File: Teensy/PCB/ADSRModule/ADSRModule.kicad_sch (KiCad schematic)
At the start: 14 parts, among them J1 Conn_02x03_Odd_Even, SW1 SW_SPDT_MSM, U1 Teensy4.0

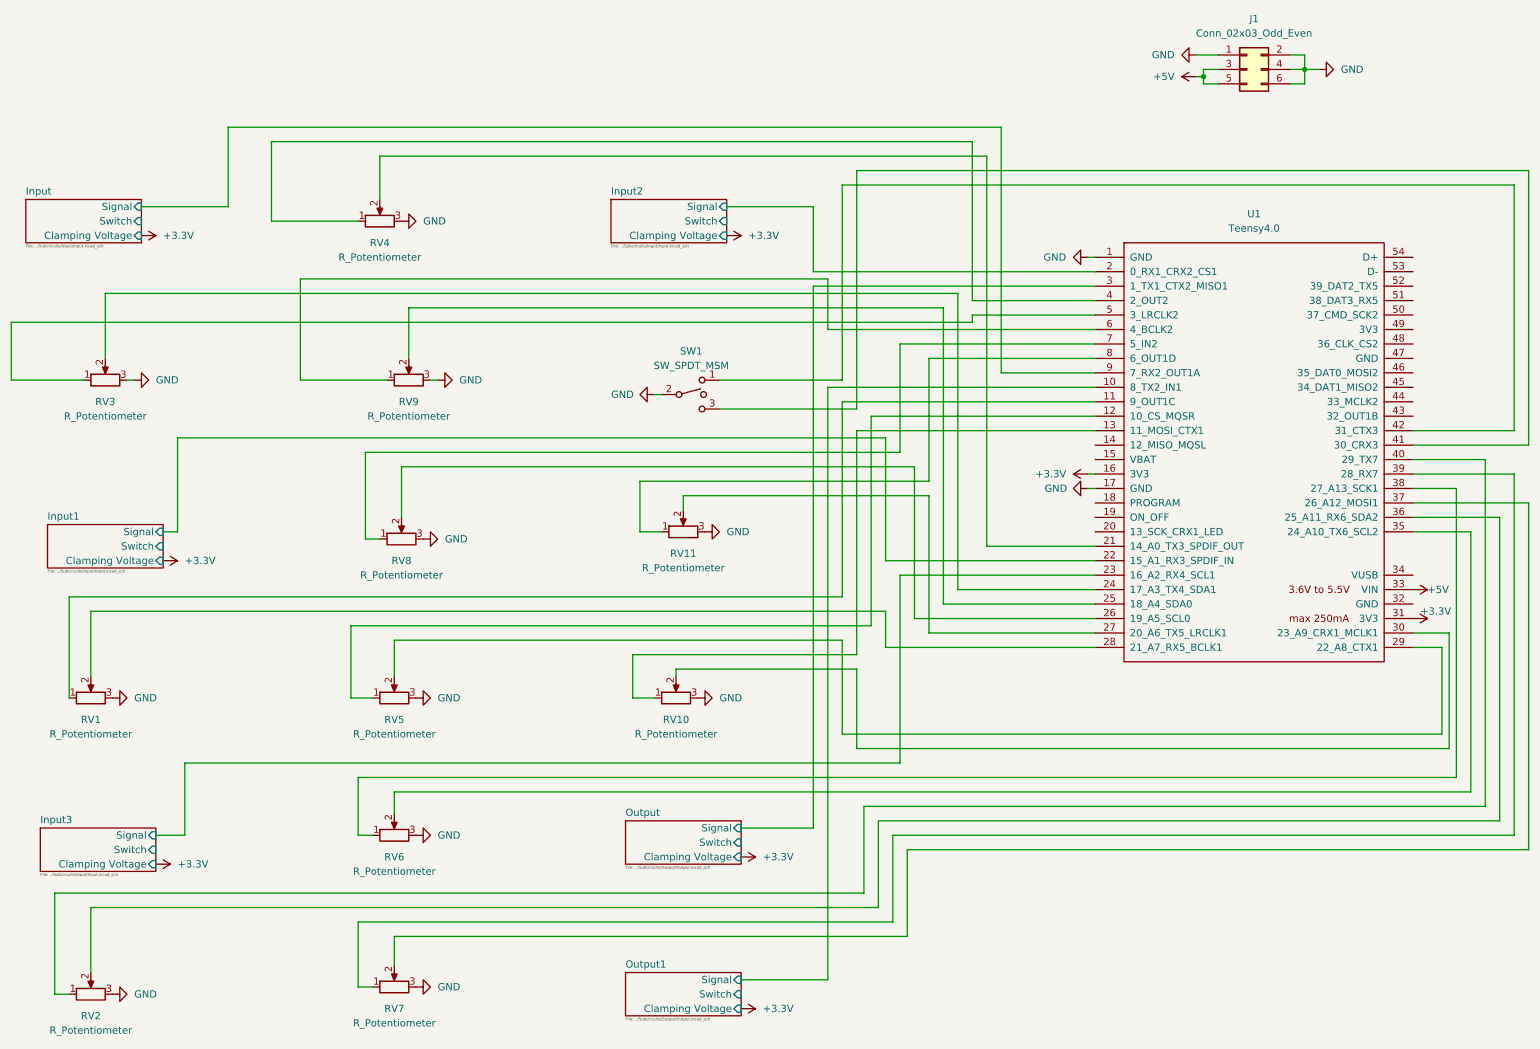
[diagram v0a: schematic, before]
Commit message: Fixed component names on schematic
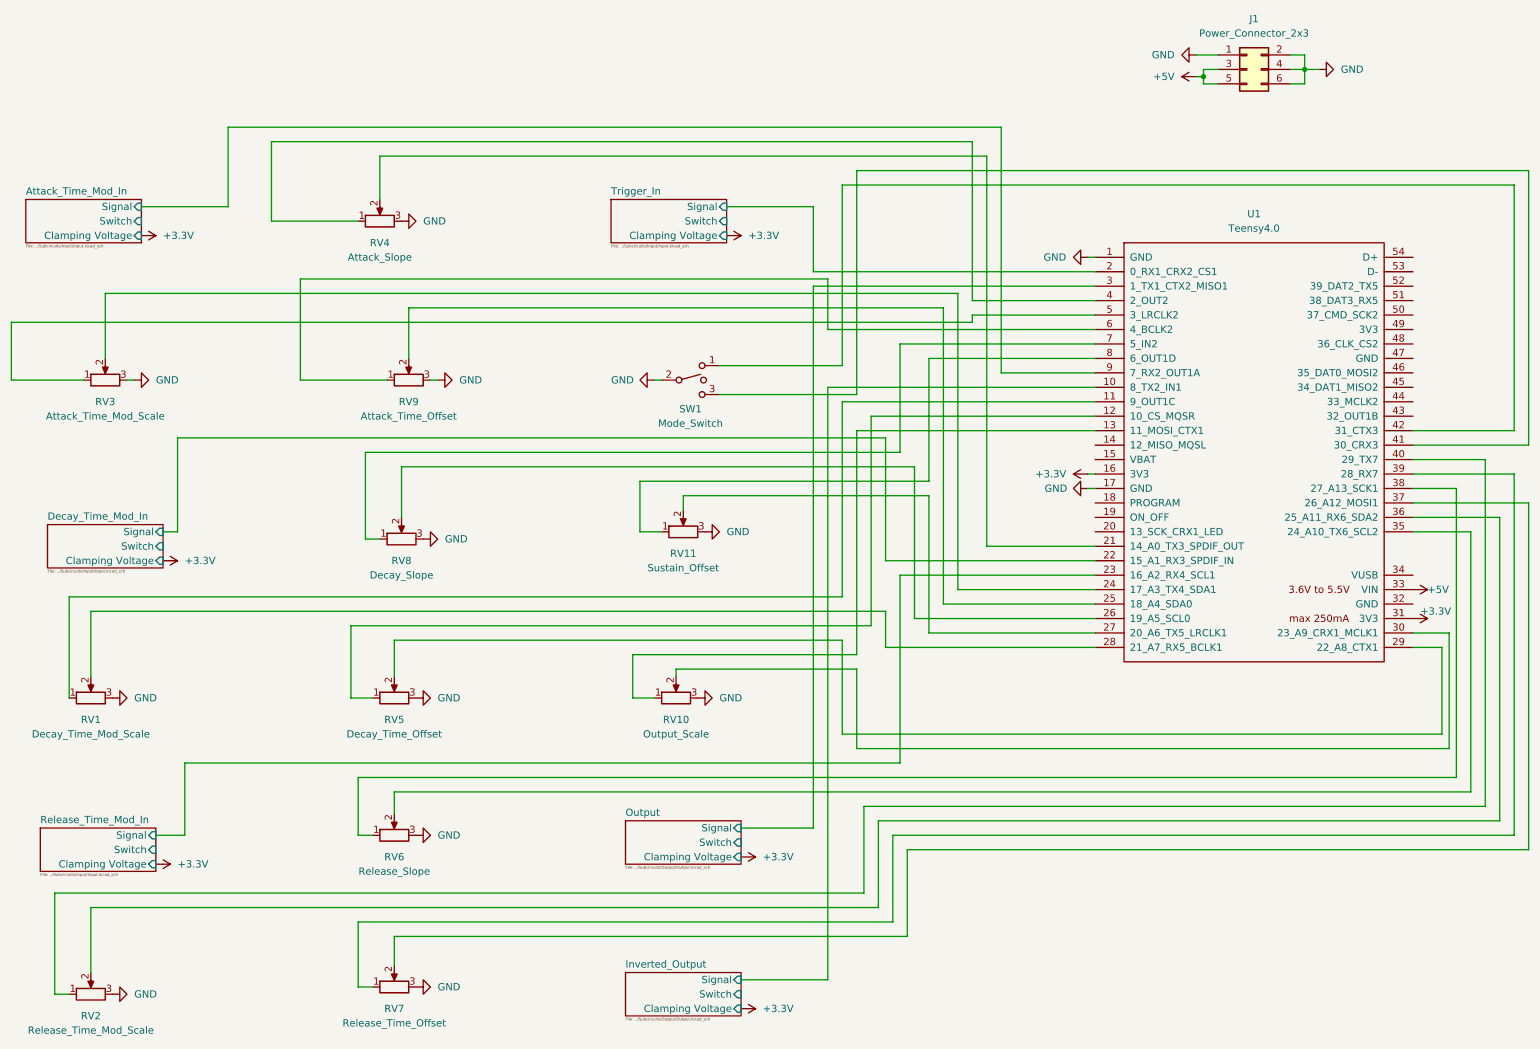
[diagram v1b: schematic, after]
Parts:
- J1: value Conn_02x03_Odd_Even -> Power_Connector_2x3
- RV1: value R_Potentiometer -> Decay_Time_Mod_Scale
- RV10: value R_Potentiometer -> Output_Scale
- RV11: value R_Potentiometer -> Sustain_Offset
- RV2: value R_Potentiometer -> Release_Time_Mod_Scale
- RV3: value R_Potentiometer -> Attack_Time_Mod_Scale
- RV4: value R_Potentiometer -> Attack_Slope
- RV5: value R_Potentiometer -> Decay_Time_Offset
- RV6: value R_Potentiometer -> Release_Slope
- RV7: value R_Potentiometer -> Release_Time_Offset
- RV8: value R_Potentiometer -> Decay_Slope
- RV9: value R_Potentiometer -> Attack_Time_Offset
- SW1: value SW_SPDT_MSM -> Mode_Switch
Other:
- sheet Input renamed Attack_Time_Mod_In
- sheet Input1 renamed Decay_Time_Mod_In
- sheet Input2 renamed Trigger_In
- sheet Input3 renamed Release_Time_Mod_In
- sheet Output1 renamed Inverted_Output
- moved on the sheet: SW1

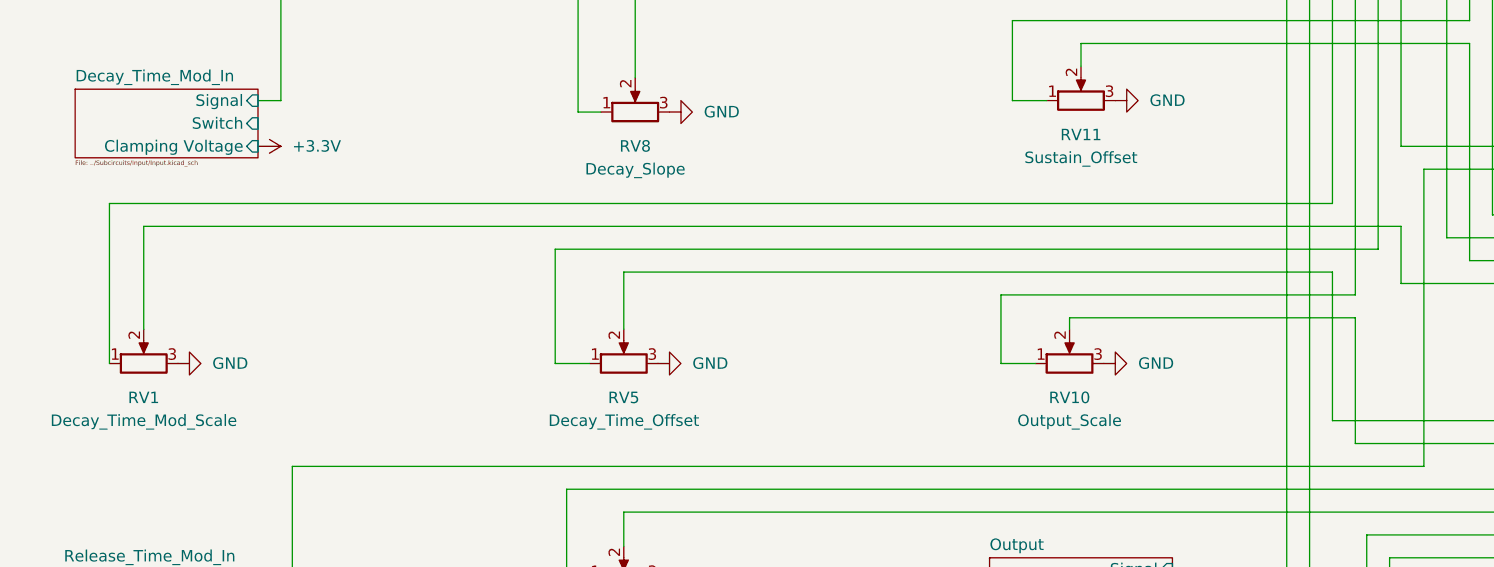
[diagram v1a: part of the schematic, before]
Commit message: Added USB_IO module PCB
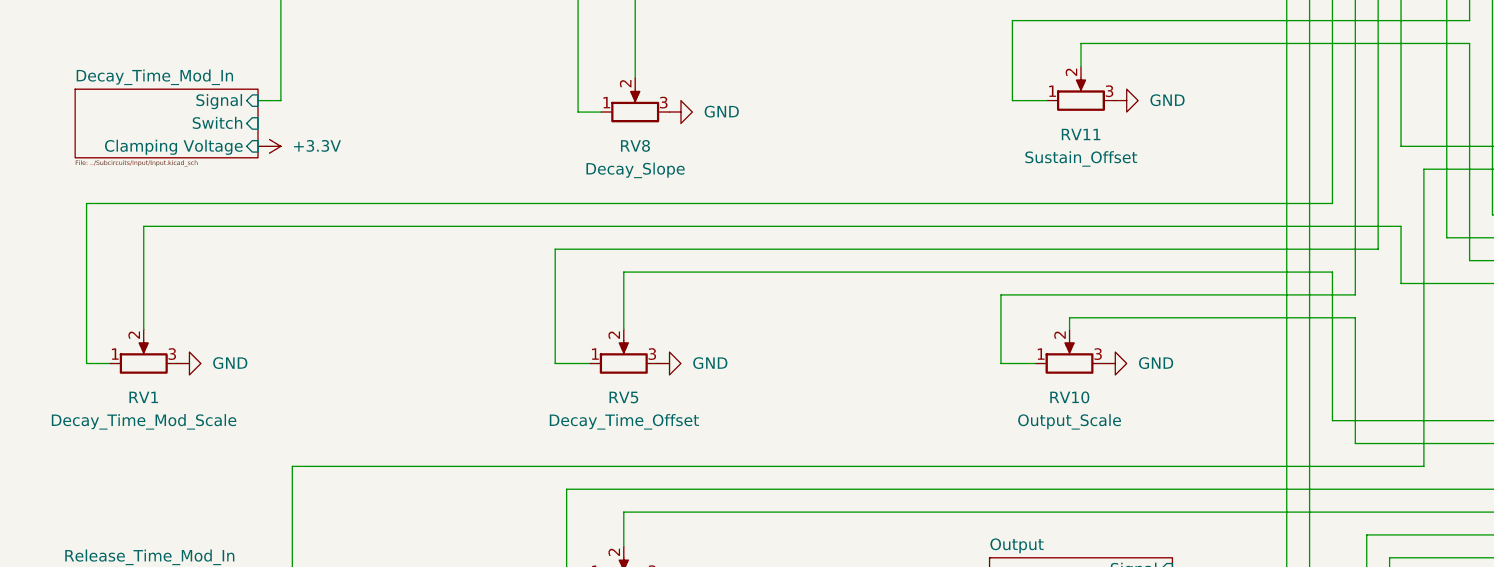
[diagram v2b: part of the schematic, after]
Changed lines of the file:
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@@
     (stroke (width 0) (type default) (color 0 0 0 0))
   )
-  (wire (pts (xy 25.4 137.16) (xy 25.4 119.38))
+  (wire (pts (xy 22.86 137.16) (xy 22.86 119.38))
     (stroke (width 0) (type default) (color 0 0 0 0))
   )
@@
     (stroke (width 0) (type default) (color 0 0 0 0))
   )
+  (wire (pts (xy 22.86 137.16) (xy 25.4 137.16))
+    (stroke (width 0) (type default) (color 0 0 0 0))
+  )
   (wire (pts (xy 35.56 81.28) (xy 36.83 81.28))
     (stroke (width 0) (type default) (color 0 0 0 0))
@@
     (stroke (width 0) (type default) (color 0 0 0 0))
   )
-  (wire (pts (xy 25.4 119.38) (xy 161.29 119.38))
-    (stroke (width 0) (type default) (color 0 0 0 0))
-  )
+  (wire (pts (xy 22.86 119.38) (xy 161.29 119.38))
+    (stroke (width 0) (type default) (color 0 0 0 0))
+  )

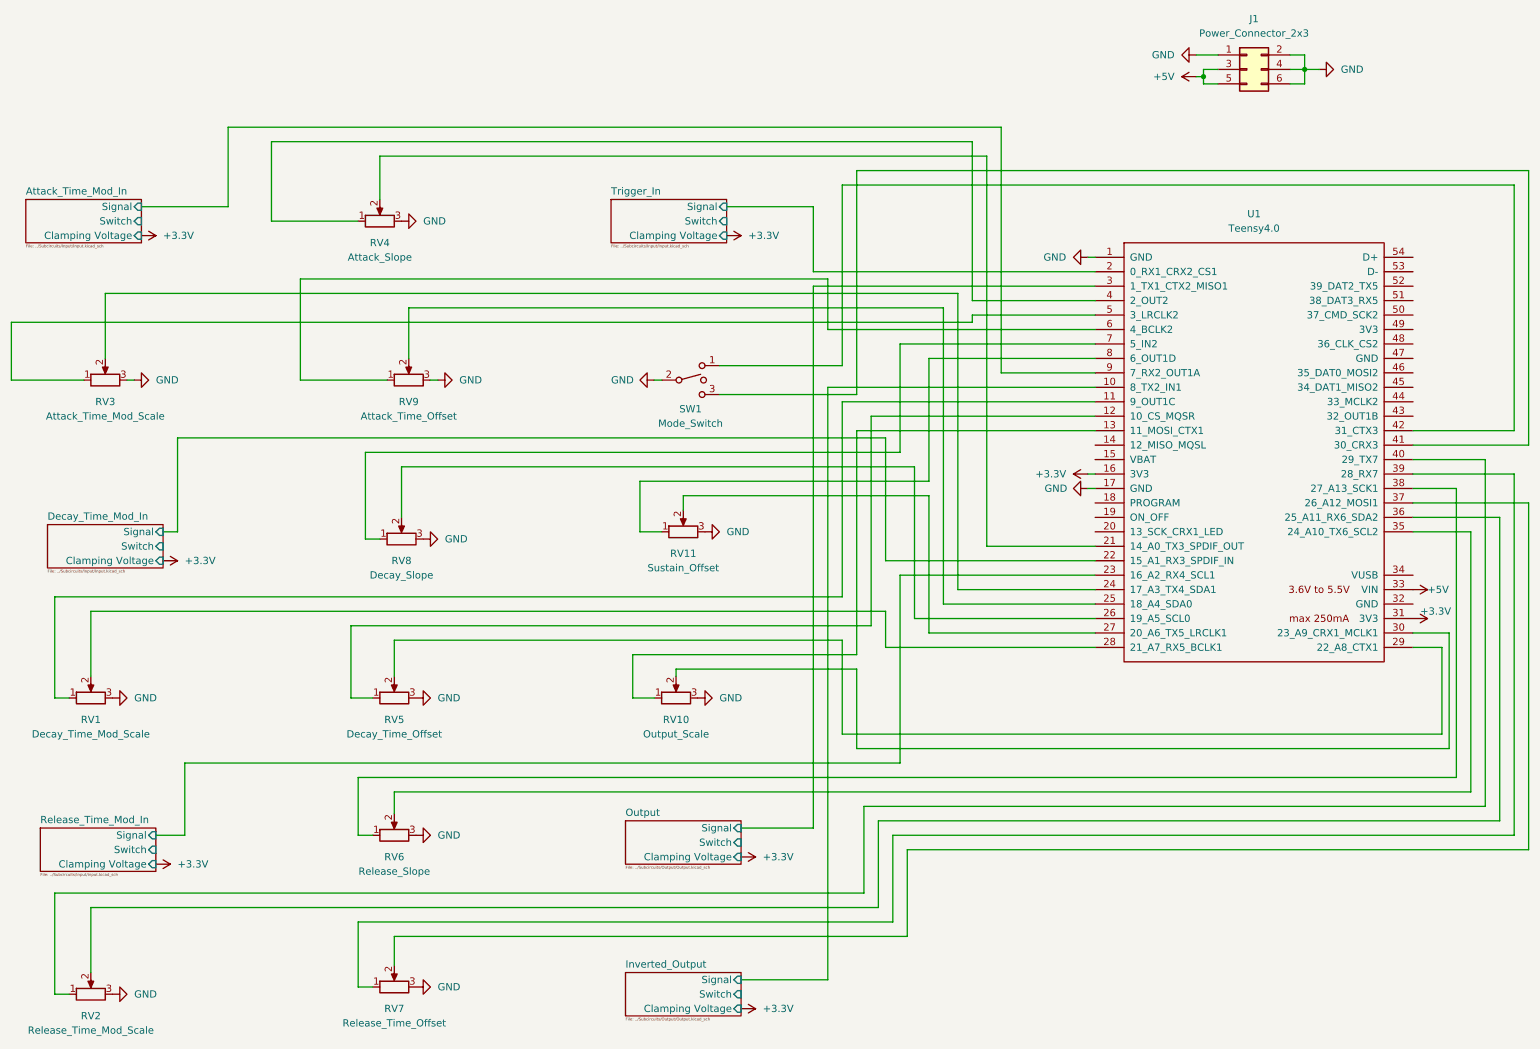
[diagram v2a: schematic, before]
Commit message: Replaced Schematic Lines with references
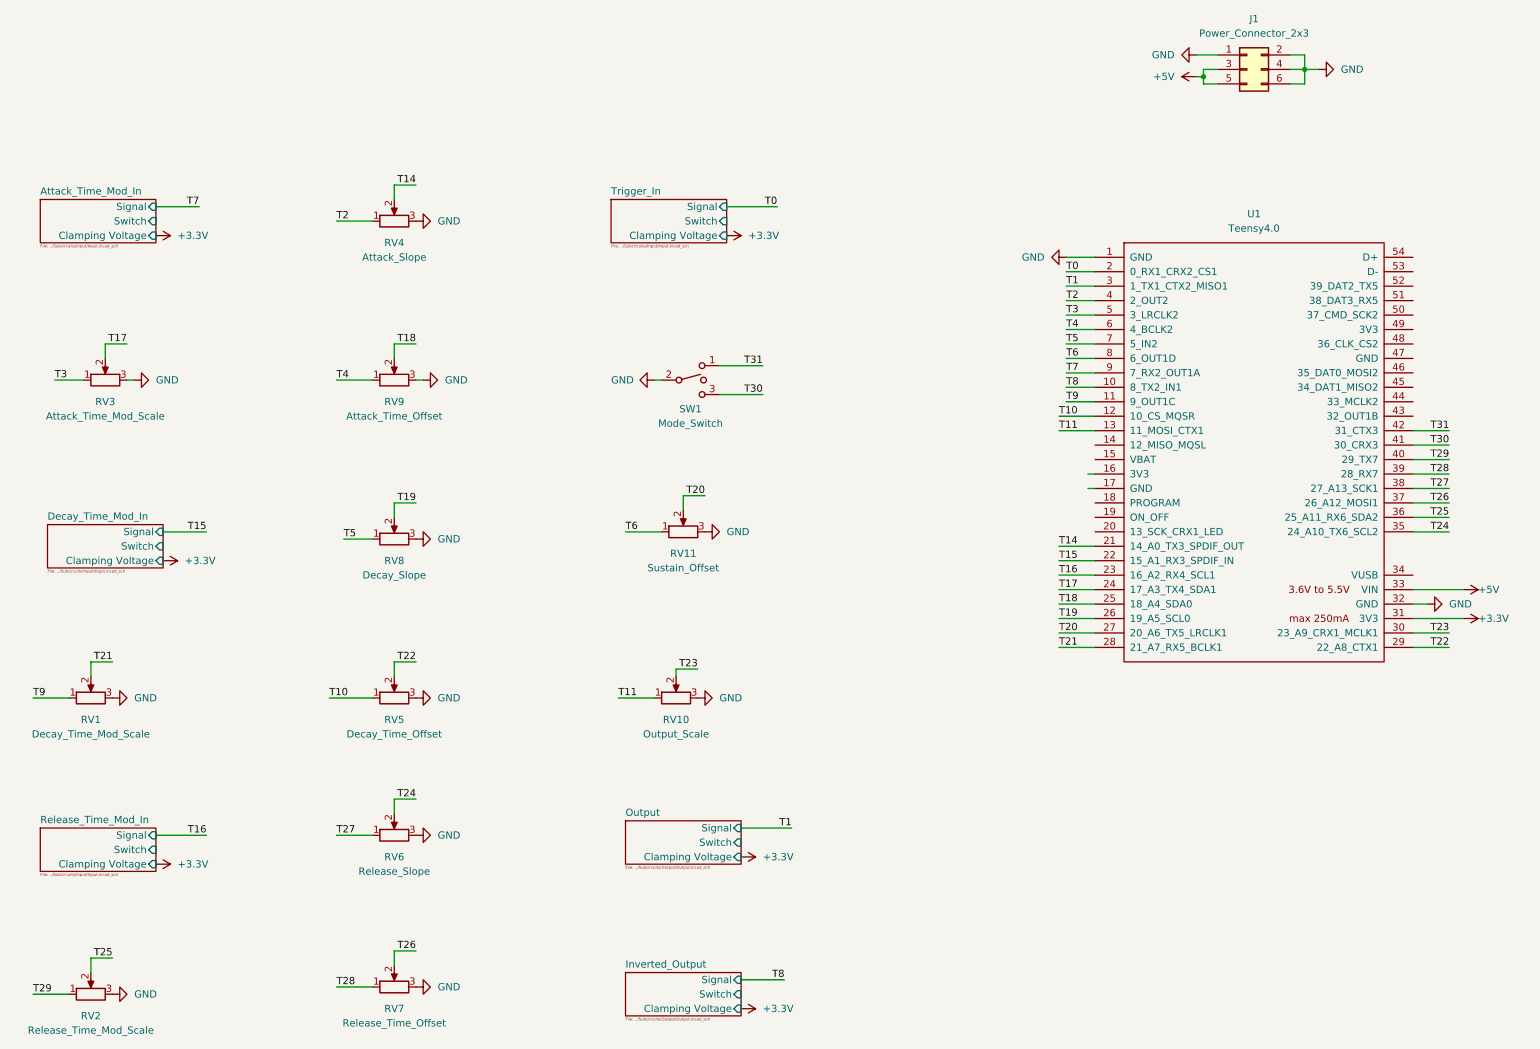
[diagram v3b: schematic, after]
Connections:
- net +3.3V: no longer U1.16 (3V3)
- net GND: now also U1.32 (GND); no longer U1.17 (GND)
- net T10: now reaches RV5.1, U1.12 (10_CS_MQSR)
- net T22: now reaches RV5.2, U1.29 (22_A8_CTX1)
- net T31: now reaches SW1.1, U1.42 (31_CTX3)
- net T30: now reaches SW1.3, U1.41 (30_CRX3)
- net T27: now reaches RV6.1, U1.38 (27_A13_SCK1)
- net T24: now reaches RV6.2, U1.35 (24_A10_TX6_SCL2)
- net T4: now reaches RV9.1, U1.6 (4_BCLK2)
- net T18: now reaches RV9.2, U1.25 (18_A4_SDA0)
- net T9: now reaches RV1.1, U1.11 (9_OUT1C)
- net T21: now reaches RV1.2, U1.28 (21_A7_RX5_BCLK1)
- net T11: now reaches RV10.1, U1.13 (11_MOSI_CTX1)
- net T14: now reaches RV4.2, U1.21 (14_A0_TX3_SPDIF_OUT)
- net T17: now reaches RV3.2, U1.24 (17_A3_TX4_SDA1)
- net T19: now reaches RV8.2, U1.26 (19_A5_SCL0)
- net T20: now reaches RV11.2, U1.27 (20_A6_TX5_LRCLK1)
- net T23: now reaches RV10.2, U1.30 (23_A9_CRX1_MCLK1)
- net T25: now reaches RV2.2, U1.36 (25_A11_RX6_SDA2)
- net T26: now reaches RV7.2, U1.37 (26_A12_MOSI1)
- net T28: now reaches RV7.1, U1.39 (28_RX7)
- net T2: now reaches RV4.1, U1.4 (2_OUT2)
- net T29: now reaches RV2.1, U1.40 (29_TX7)
- net T3: now reaches RV3.1, U1.5 (3_LRCLK2)
- net T5: now reaches RV8.1, U1.7 (5_IN2)
- net T6: now reaches RV11.1, U1.8 (6_OUT1D)
- net Attack_Time_Mod_In/Signal renamed T7
- net Decay_Time_Mod_In/Signal renamed T15
- net Inverted_Output/Signal renamed T8
- net Output/Signal renamed T1
- net Release_Time_Mod_In/Signal renamed T16
- net Trigger_In/Signal renamed T0
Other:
- moved on the sheet: RV4, RV8, RV9
